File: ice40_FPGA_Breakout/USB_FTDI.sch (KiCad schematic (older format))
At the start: 52 parts, among them J1 USB_B_Micro, J2 3pos_Jumper, J3 3pos_Jumper, U5 93LCxxC, U6 FT2232H, Y1 ABM10AIG-12.000MHZ-4Z-T3

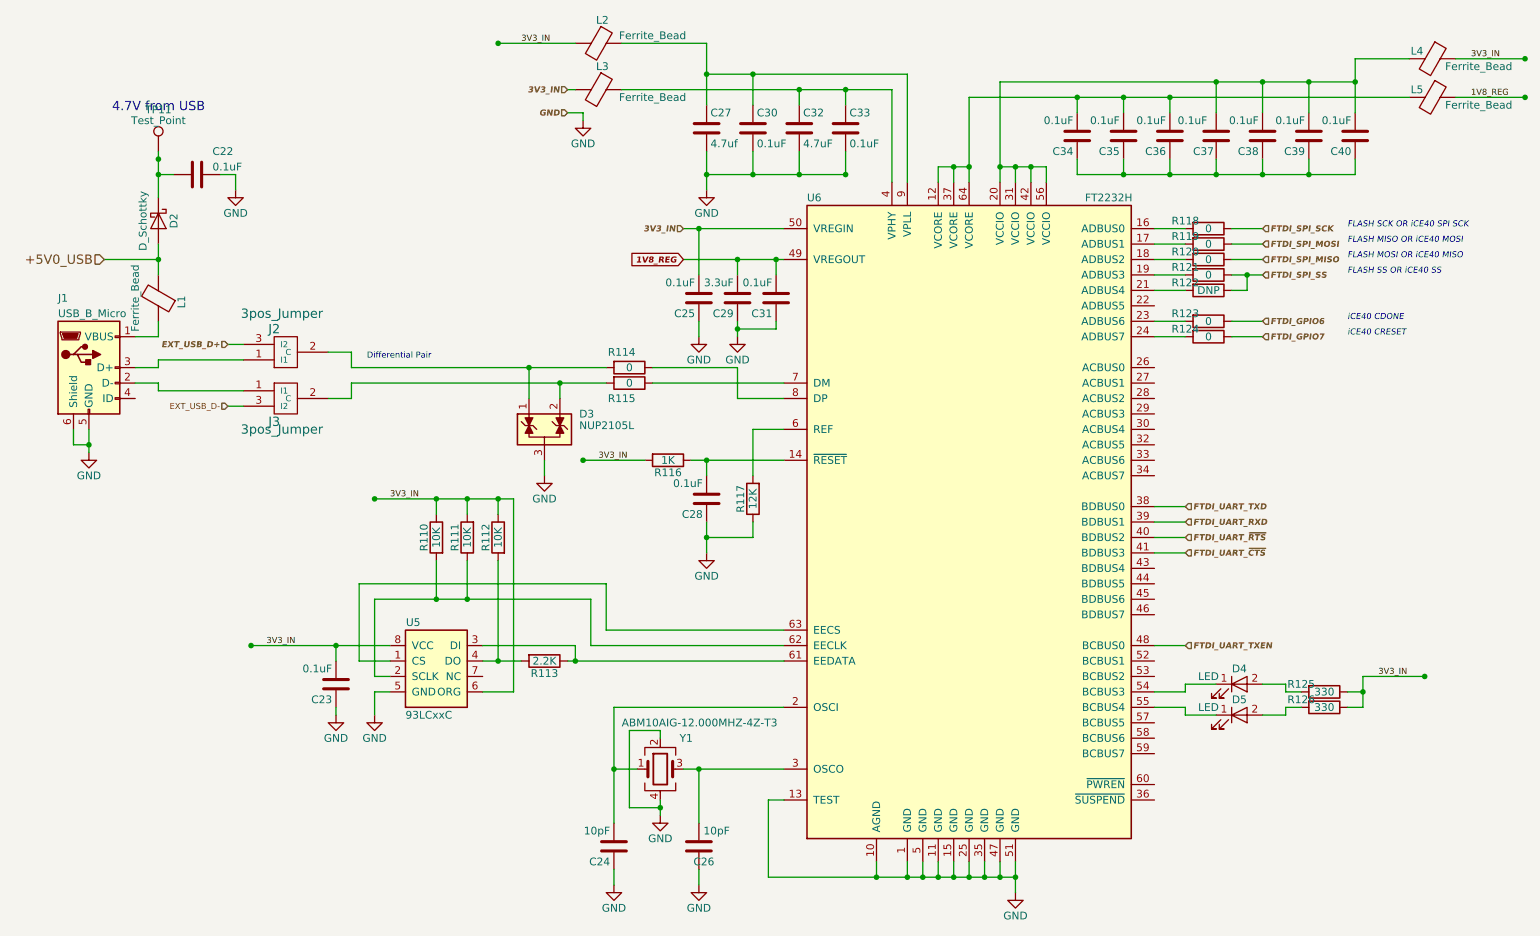
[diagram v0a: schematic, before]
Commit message: schematic clean up, label aligned
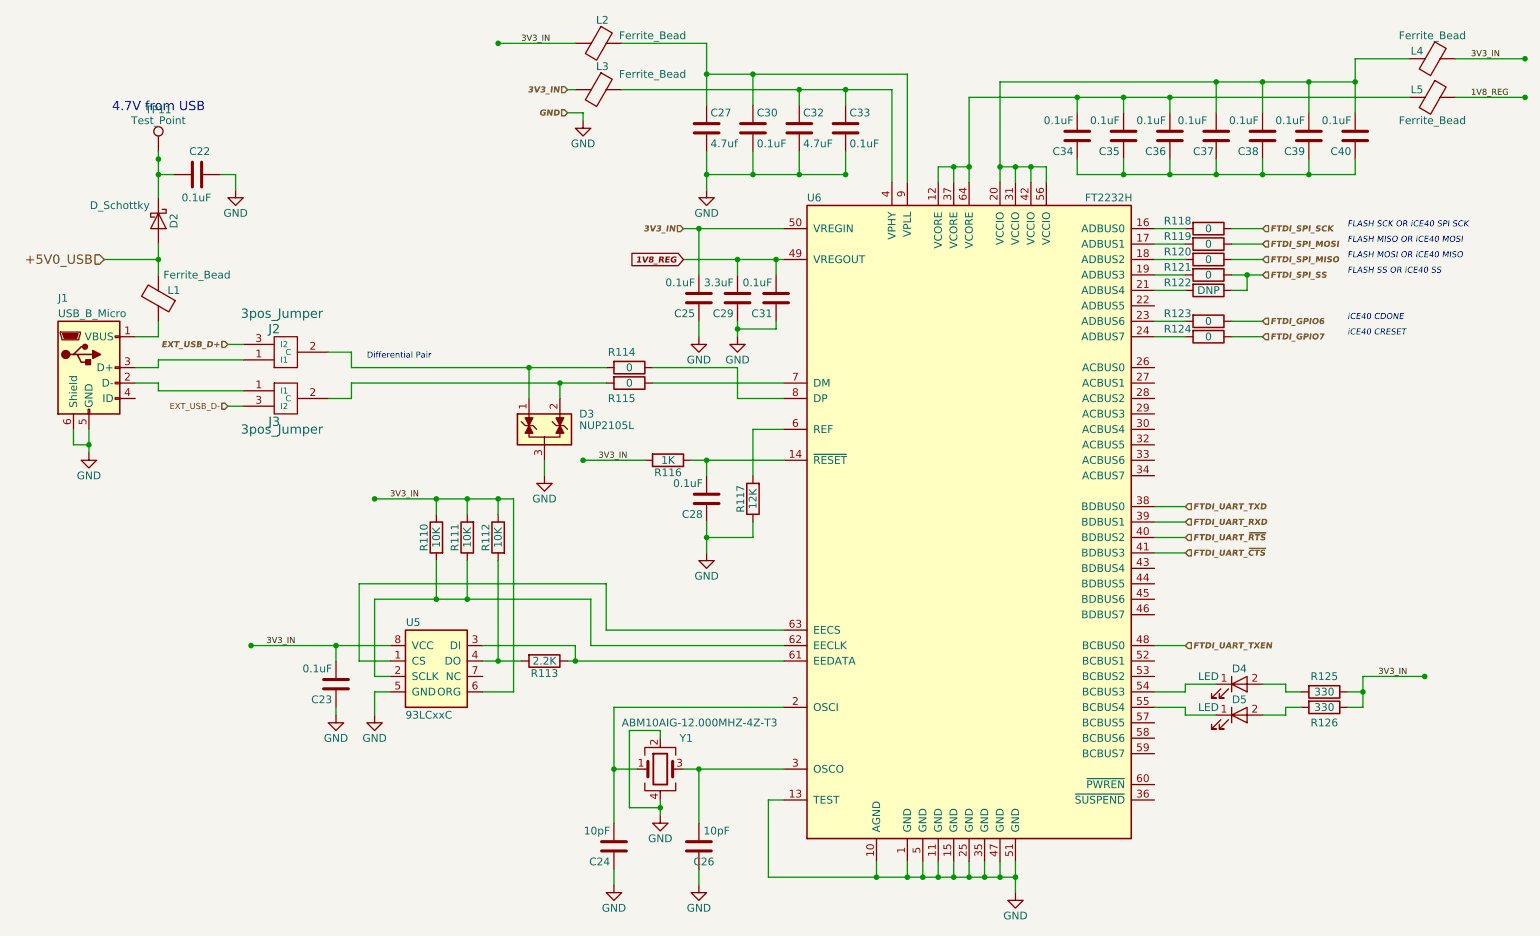
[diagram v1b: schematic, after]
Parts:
- C22, C23, C25, C26, C28, C30, C31, C33, C34, C35, C36, C37, C38, C39, C40: footprint (none) -> Capacitor_SMD:C_0402_1005Metric
- C24, C27, C29, C32: footprint (none) -> Capacitor_SMD:C_0603_1608Metric
- D4, D5: footprint (none) -> LED_SMD:LED_0402_1005Metric
- J2, J3: footprint (none) -> Conn_PinHeader_2.00mm:PinHeader_1x03_P2.00mm_Vertical
- R110, R111, R112, R113, R114, R115, R116, R117, R118, R119, R120, R121, R122, R123, R124, R125, R126: footprint (none) -> Resistor_SMD:R_0402_1005Metric
- TP11: footprint (none) -> Conn_PinHeader_2.00mm:PinHeader_1x01_P2.00mm_Vertical

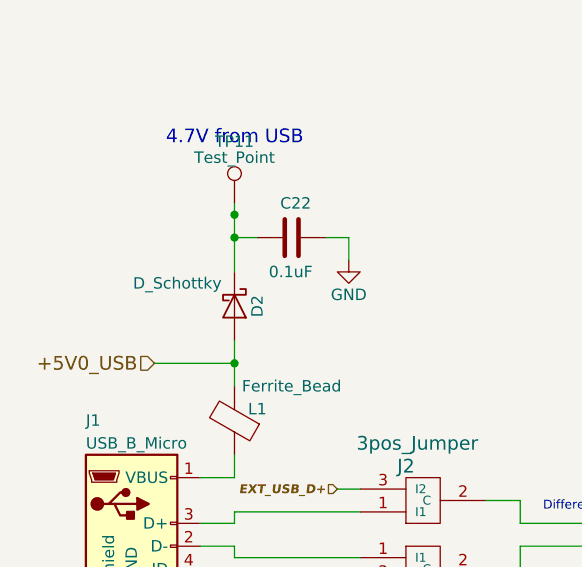
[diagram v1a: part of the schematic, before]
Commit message: assigned footprint to each component
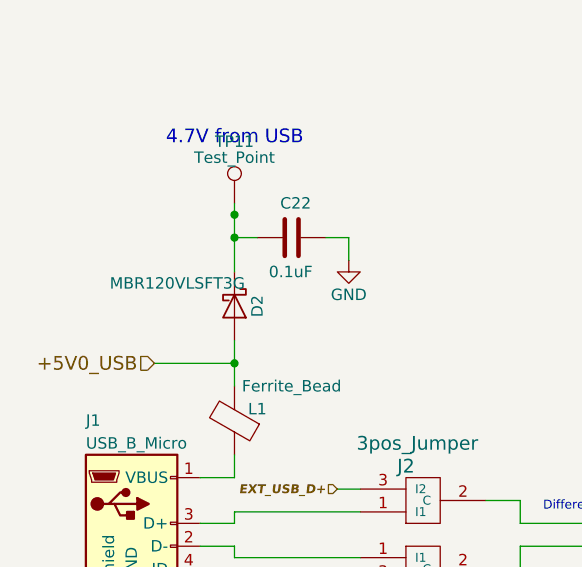
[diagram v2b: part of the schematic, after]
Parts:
- D2: value D_Schottky -> MBR120VLSFT3G; footprint (none) -> Diode_SMD:D_SOD-123F
- D3: footprint TO_SOT_Packages_SMD:SOT-23 -> Package_TO_SOT_SMD:SOT-23
- J1: footprint (none) -> Connector_USB:USB_Micro-B_GCT_USB3076-30-A
- J2, J3: footprint Conn_PinHeader_2.00mm:PinHeader_1x03_P2.00mm_Vertical -> Connector_PinHeader_2.00mm:PinHeader_1x03_P2.00mm_Vertical
- L1, L2, L3, L4, L5: footprint (none) -> Inductor_SMD:L_0603_1608Metric
- TP11: footprint Conn_PinHeader_2.00mm:PinHeader_1x01_P2.00mm_Vertical -> TestPoint:TestPoint_Pad_D2.0mm
- U5: footprint (none) -> Package_SO:SOIC-8_3.9x4.9mm_P1.27mm
- U6: footprint (none) -> Package_DFN_QFN:QFN-64-1EP_9x9mm_P0.5mm_EP7.35x7.35mm
- Y1: footprint (none) -> Crystal:Crystal_SMD_Abracon_ABM10-4Pin_2.5x2.0mm
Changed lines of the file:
@@
 F 0 "J1" H 1350 3200 50  0000 L CNN
 F 1 "USB_B_Micro" H 1350 3100 50  0000 L CNN
-F 2 "" H 1700 2700 50  0001 C CNN
+F 2 "Connector_USB:USB_Micro-B_GCT_USB3076-30-A" H 1700 2700 50  0001 C CNN
 F 3 "" H 1700 2700 50  0001 C CNN
 	1    1550 2750
@@
 F 0 "D3" H 4725 3250 50  0000 L CNN
 F 1 "NUP2105L" H 4725 3175 50  0000 L CNN
-F 2 "TO_SOT_Packages_SMD:SOT-23" H 4725 3100 50  0001 L CNN
+F 2 "Package_TO_SOT_SMD:SOT-23" H 4725 3100 50  0001 L CNN
 F 3 "" H 4625 3275 50  0001 C CNN
 	1    4500 3150
@@
 F 0 "L2" V 4700 675 50  0000 C CNN
 F 1 "Ferrite_Bead" V 4800 1000 50  0000 C CNN
-F 2 "" V 4780 650 50  0001 C CNN
+F 2 "Inductor_SMD:L_0603_1608Metric" V 4780 650 50  0001 C CNN
 F 3 "" H 4850 650 50  0001 C CNN
 	1    4850 650
@@
 F 0 "L3" V 4700 975 50  0000 C CNN
 F 1 "Ferrite_Bead" V 4750 1300 50  0000 C CNN
-F 2 "" V 4780 950 50  0001 C CNN
+F 2 "Inductor_SMD:L_0603_1608Metric" V 4780 950 50  0001 C CNN
 F 3 "" H 4850 950 50  0001 C CNN
 	1    4850 950
@@
 F 0 "L4" V 10200 650 50  0000 C CNN
 F 1 "Ferrite_Bead" V 10100 750 50  0000 C CNN
-F 2 "" V 10180 750 50  0001 C CNN
+F 2 "Inductor_SMD:L_0603_1608Metric" V 10180 750 50  0001 C CNN
 F 3 "" H 10250 750 50  0001 C CNN
 	1    10250 750
@@
 F 0 "L1" H 1900 2250 50  0000 C CNN
 F 1 "Ferrite_Bead" H 1750 2150 50  0000 C CNN
-F 2 "" V 1930 2300 50  0001 C CNN
+F 2 "Inductor_SMD:L_0603_1608Metric" V 1930 2300 50  0001 C CNN
 F 3 "" H 2000 2300 50  0001 C CNN
 	1    2000 2300
@@
 F 0 "L5" V 10200 900 50  0000 C CNN
 F 1 "Ferrite_Bead" V 10400 1000 50  0000 C CNN
-F 2 "" V 10180 1000 50  0001 C CNN
+F 2 "Inductor_SMD:L_0603_1608Metric" V 10180 1000 50  0001 C CNN
 F 3 "" H 10250 1000 50  0001 C CNN
 	1    10250 1000
@@
 F 0 "U6" H 6200 5850 50  0000 L CNN
 F 1 "FT2232H" H 8000 5850 50  0000 L CNN
-F 2 "" H 7250 3750 50  0001 C CNN
+F 2 "Package_DFN_QFN:QFN-64-1EP_9x9mm_P0.5mm_EP7.35x7.35mm" H 7250 3750 50  0001 C CNN
 F 3 "" H 7250 3750 50  0001 C CNN
 	1    7250 3750
@@
 F 0 "U5" H 3650 5100 50  0000 C CNN
 F 1 "93LCxxC" H 3600 4500 50  0000 L CNN
-F 2 "" H 3700 4750 50  0001 C CNN
+F 2 "Package_SO:SOIC-8_3.9x4.9mm_P1.27mm" H 3700 4750 50  0001 C CNN
 F 3 "" H 3800 4850 50  0001 C CNN
 	1    3800 4750
@@
 P 2000 1800
 F 0 "D2" H 2000 1900 50  0000 C CNN
-F 1 "D_Schottky" V 1900 1550 50  0000 C CNN
-F 2 "" H 2000 1800 50  0001 C CNN
+F 1 " MBR120VLSFT3G " V 1900 1550 50  0000 C CNN
+F 2 "Diode_SMD:D_SOD-123F" H 2000 1800 50  0001 C CNN
 F 3 "" H 2000 1800 50  0001 C CNN
 	1    2000 1800
@@
 F 0 "Y1" H 5375 5550 50  0000 L CNN
 F 1 "ABM10AIG-12.000MHZ-4Z-T3 " H 5000 5650 50  0000 L CNN
-F 2 "" H 5250 5350 50  0001 C CNN
+F 2 "Crystal:Crystal_SMD_Abracon_ABM10-4Pin_2.5x2.0mm" H 5250 5350 50  0001 C CNN
 F 3 "" H 5250 5350 50  0001 C CNN
 	1    5250 5350
@@
 F 0 "J3" H 2750 3100 60  0000 C CNN
 F 1 "3pos_Jumper" H 2800 3150 60  0000 C CNN
-F 2 "Conn_PinHeader_2.00mm:PinHeader_1x03_P2.00mm_Vertical" H 2800 2900 60  0001 C CNN
+F 2 "Connector_PinHeader_2.00mm:PinHeader_1x03_P2.00mm_Vertical" H 2800 2900 60  0001 C CNN
 F 3 "" H 2800 2900 60  0001 C CNN
 	1    2800 2900
@@
 F 0 "J2" H 2750 2900 60  0000 C CNN
 F 1 "3pos_Jumper" H 2800 3000 60  0000 C CNN
-F 2 "Conn_PinHeader_2.00mm:PinHeader_1x03_P2.00mm_Vertical" H 2800 2700 60  0001 C CNN
+F 2 "Connector_PinHeader_2.00mm:PinHeader_1x03_P2.00mm_Vertical" H 2800 2700 60  0001 C CNN
 F 3 "" H 2800 2700 60  0001 C CNN
 	1    2800 2700
@@
 F 0 "TP11" H 2000 1620 50  0000 C CNN
 F 1 "Test_Point" H 2000 1550 50  0000 C CNN
-F 2 "Conn_PinHeader_2.00mm:PinHeader_1x01_P2.00mm_Vertical" H 2200 1350 50  0001 C CNN
+F 2 "TestPoint:TestPoint_Pad_D2.0mm" H 2200 1350 50  0001 C CNN
 F 3 "" H 2200 1350 50  0001 C CNN
 	1    2000 1350

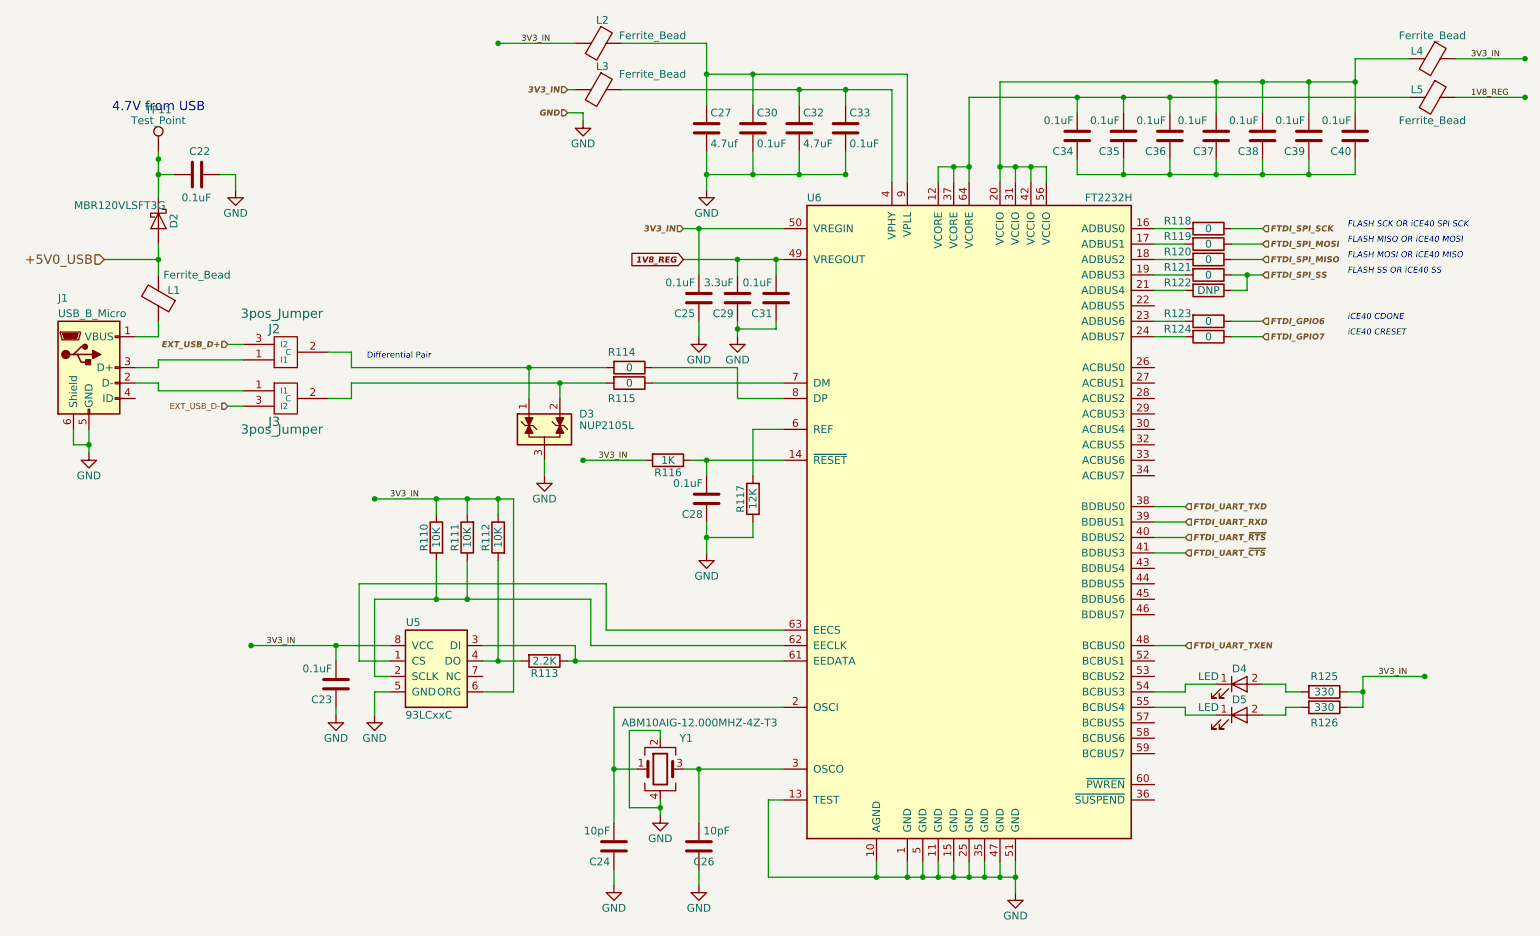
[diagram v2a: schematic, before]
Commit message: ftdi component placement
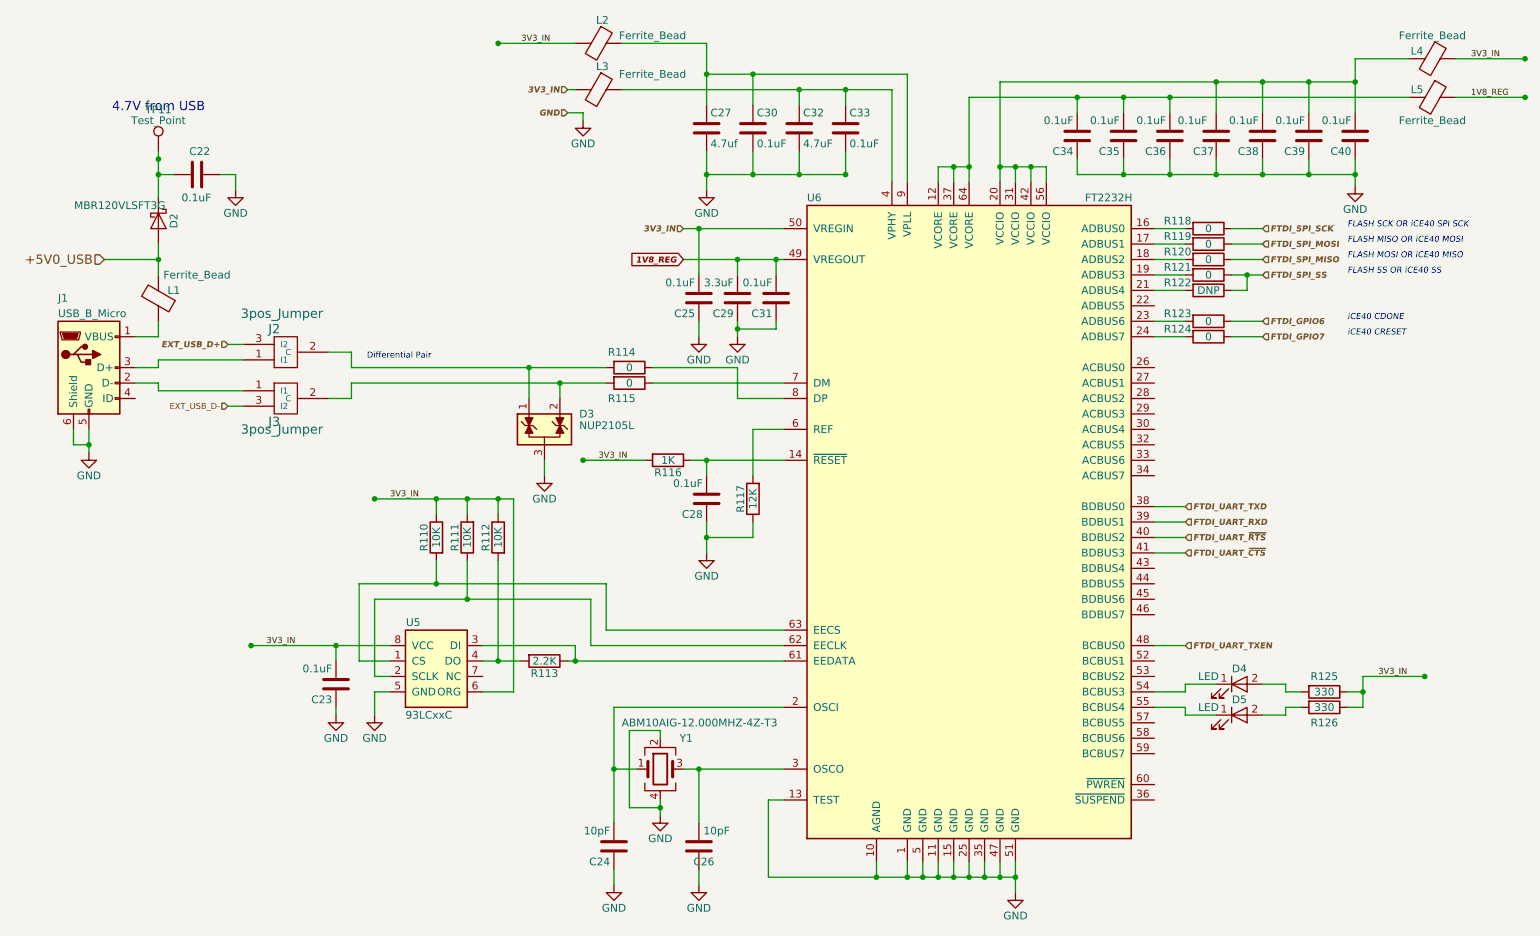
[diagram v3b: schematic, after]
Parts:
- C24: footprint Capacitor_SMD:C_0603_1608Metric -> Capacitor_SMD:C_0402_1005Metric
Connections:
- net GND: now also C34.1, C35.1, C36.1, C37.2, C38.1, C39.1, C40.1
- net at R111.1, U5.2 (SCLK), U6.62 (EECLK): no longer R110.2
- net at U5.1 (CS), U6.63 (EECS): now also R110.2
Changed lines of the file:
@@
 F 0 "C24" H 4975 5950 50  0000 L CNN
 F 1 "10pF" H 4975 5750 50  0000 L CNN
-F 2 "Capacitor_SMD:C_0603_1608Metric" H 4988 5700 50  0001 C CNN
+F 2 "Capacitor_SMD:C_0402_1005Metric" H 4988 5700 50  0001 C CNN
 F 3 "" H 4950 5850 50  0001 C CNN
 	1    4950 5850
@@
 	3400 4750 3400 4250
 Wire Wire Line
-	3800 4000 3800 4250
-Connection ~ 3800 4250
-Wire Wire Line
 	4000 4250 4000 4000
 Connection ~ 4000 4250
@@
 Connection ~ 8250 1500
 Wire Wire Line
-	9750 1500 9750 1400
+	9750 1400 9750 1575
 Connection ~ 8550 1500
 Wire Wire Line
@@
 3V3_IN
 Connection ~ 4750 3350
+$Comp
+L GND #PWR036
+U 1 1 5ACC1320
+P 9750 1575
+F 0 "#PWR036" H 9750 1325 50  0001 C CNN
+F 1 "GND" H 9750 1425 50  0000 C CNN
+F 2 "" H 9750 1575 50  0001 C CNN
+F 3 "" H 9750 1575 50  0001 C CNN
+	1    9750 1575
+	1    0    0    -1
+$EndComp
+Connection ~ 9750 1500
+Wire Wire Line
+	3800 4000 3800 4150
+Connection ~ 3800 4150
 $EndSCHEMATC
